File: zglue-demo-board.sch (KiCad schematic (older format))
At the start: 101 parts, among them J10 0473460001, J2 DF13A-2P-1.25H, J3 20021121-00010C4LF, J4 2x20_Header_Female, J5 0473460001, J6 556500488, J7 556500488, J8 WE_686115148922, J9 WE_686115148922, U1 LD1117S33CTR, U2 NTB0104BQ, U3 NTB0104BQ, U4 NTB0104BQ, U5 93LC56CT-IMC, U6 FT4232HQ, Y1 ASFLMB-12.000MHZ-LC-T

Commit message: finished initial component placement, some minor changes in schematics related to footprints
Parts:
- removed C4: C_100n_0402_6V3, antmicro-footprints:0402-cap, symbol antmicroCapacitors0402:C_100n_0402_6V3
- removed C5: C_10u_0603, antmicro-footprints:0603-cap, symbol antmicroCapacitors0603:C_10u_0603
- removed J9: WE_686115148922, antmicro-footprints:WE_686115148922, symbol antmicroFCCConnectors:WE_686115148922
- removed U1: LD1117S33CTR, antmicro-footprints:SOT-223, symbol antmicroPMICVoltageRegulatorsLinear:LD1117S33CTR
- added C4, C5: C_1u_0603, antmicro-footprints:0603-cap, symbol antmicroCapacitors0603:C_1u_0603
- added J9: WE_686115148922_FLIPPED, antmicro-footprints:WE_686115148922_FLIPPED, symbol antmicroFCCConnectors:WE_686115148922_FLIPPED
- added N1: antmicro_logo, antmicro-footprints:antmicro-logo_scaled_20mm, symbol antmicroMechanicalParts:antmicro_logo
- added U1: MCP1700T-3302E_TT, antmicro-footprints:SOT-23-3, symbol antmicroPMICVoltageRegulatorsLinear:MCP1700T-3302E_TT
- FB1, FB2: footprint antmicro-footprints:0603 -> antmicro-footprints:0603-res
- JP1, JP2, JP3: footprint (none) -> Jumper:SolderJumper-3_P1.3mm_Open_Pad1.0x1.5mm
- U5: footprint antmicro-footprints:SOIC-8_W3.9mm -> antmicro-footprints:DFN-8_2x3mm
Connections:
- net labels added: CTRL_RST_FLASH_SOC_CS_3V3
- net labels removed: CTRL_RST, CTRL_RST_3V3
- wire segments 421 -> 418
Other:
- note added: "TODO: check i2c connection\n"
- note added: "Voltage level selection"
- note removed: "TODO: check pin order, check i2c connection\n"
- moved on the sheet: JP1, JP2, JP3, TP5, TP6, TP7

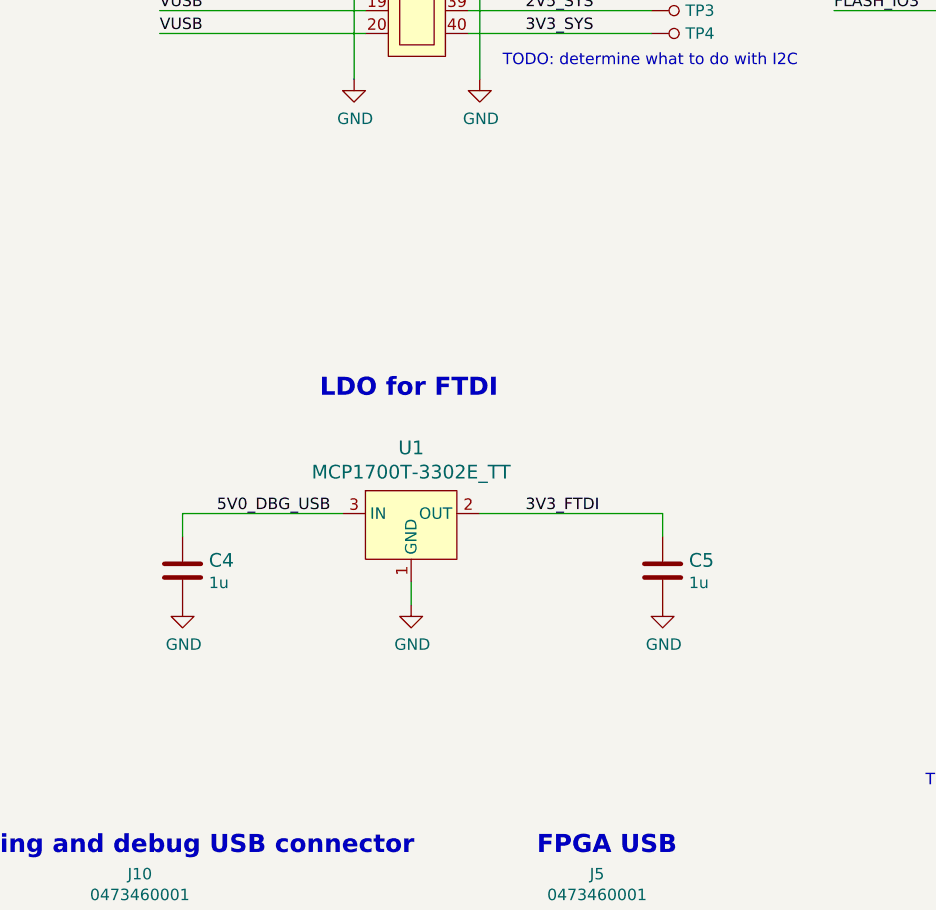
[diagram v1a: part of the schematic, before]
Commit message: added programming header for QSPI flash
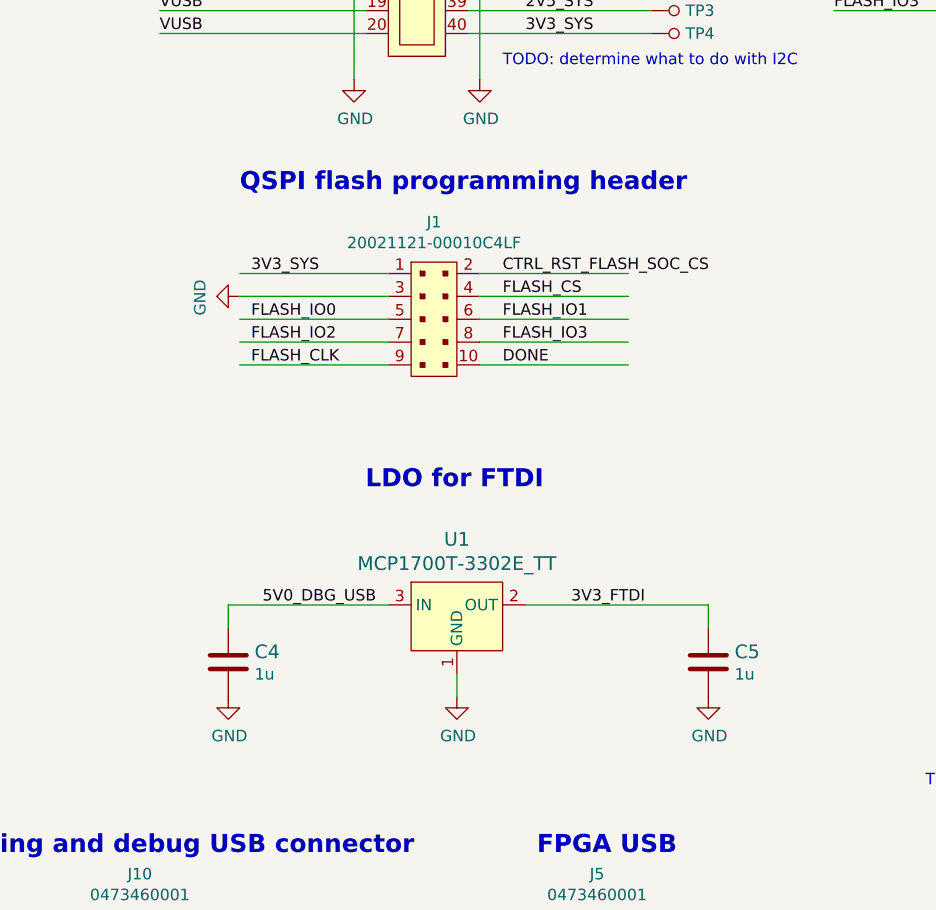
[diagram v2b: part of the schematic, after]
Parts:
- added J1: 20021121-00010C4LF, antmicro-footprints:PinHeader_2x5_P1.27mm, symbol antmicroRectangularConnectorsHeadersMalePins:20021121-00010C4LF
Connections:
- wire segments 418 -> 428
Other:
- note added: "QSPI flash programming header"
- moved on the sheet: C4, C5, U1
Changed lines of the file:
@@
 EESchema Schematic File Version 4
-LIBS:zglue-demo-board-cache
 EELAYER 26 0
 EELAYER END
@@
 L power:GND #PWR07
 U 1 1 5E3C7E24
-P 11400 6000
-F 0 "#PWR07" H 11400 5750 50  0001 C CNN
-F 1 "GND" H 11405 5827 50  0000 C CNN
-F 2 "" H 11400 6000 50  0001 C CNN
-F 3 "" H 11400 6000 50  0001 C CNN
-	1    11400 6000
+P 11600 6400
+F 0 "#PWR07" H 11600 6150 50  0001 C CNN
+F 1 "GND" H 11605 6227 50  0000 C CNN
+F 2 "" H 11600 6400 50  0001 C CNN
+F 3 "" H 11600 6400 50  0001 C CNN
+	1    11600 6400
 	1    0    0    -1
 $EndComp
 Wire Wire Line
-	11400 5900 11400 6000
-Text Label 10550 5600 0    50   ~ 0
+	11600 6300 11600 6400
+Text Label 10750 6000 0    50   ~ 0
 5V0_DBG_USB
-Text Label 11900 5600 0    50   ~ 0
+Text Label 12100 6000 0    50   ~ 0
 3V3_FTDI
-Text Notes 11000 5100 0    79   ~ 16
+Text Notes 11200 5500 0    79   ~ 16
 LDO for FTDI
 $Comp
 L power:GND #PWR06
 U 1 1 5E4D1E3B
-P 10400 6000
-F 0 "#PWR06" H 10400 5750 50  0001 C CNN
-F 1 "GND" H 10405 5827 50  0000 C CNN
-F 2 "" H 10400 6000 50  0001 C CNN
-F 3 "" H 10400 6000 50  0001 C CNN
-	1    10400 6000
+P 10600 6400
+F 0 "#PWR06" H 10600 6150 50  0001 C CNN
+F 1 "GND" H 10605 6227 50  0000 C CNN
+F 2 "" H 10600 6400 50  0001 C CNN
+F 3 "" H 10600 6400 50  0001 C CNN
+	1    10600 6400
 	1    0    0    -1
 $EndComp
@@
 L power:GND #PWR012
 U 1 1 5E4D1F0E
-P 12500 6000
-F 0 "#PWR012" H 12500 5750 50  0001 C CNN
-F 1 "GND" H 12505 5827 50  0000 C CNN
-F 2 "" H 12500 6000 50  0001 C CNN
-F 3 "" H 12500 6000 50  0001 C CNN
-	1    12500 6000
+P 12700 6400
+F 0 "#PWR012" H 12700 6150 50  0001 C CNN
+F 1 "GND" H 12705 6227 50  0000 C CNN
+F 2 "" H 12700 6400 50  0001 C CNN
+F 3 "" H 12700 6400 50  0001 C CNN
+	1    12700 6400
 	1    0    0    -1
 $EndComp
 Wire Wire Line
-	10400 5600 11100 5600
+	10600 6000 11300 6000
 $Comp
 L antmicroDiodesRectifiersSingle:MBR0540T1G D1
@@
 L antmicroPMICVoltageRegulatorsLinear:MCP1700T-3302E_TT U1
 U 1 1 5DD3D3B5
-P 11400 5600
-F 0 "U1" H 11400 5887 60  0000 C CNN
-F 1 "MCP1700T-3302E_TT" H 11400 5781 60  0000 C CNN
-F 2 "antmicro-footprints:SOT-23-3" H 11600 5800 60  0001 L CNN
-F 3 "http://www.microchip.com/mymicrochip/filehandler.aspx?ddocname=en011779" H 11600 5900 60  0001 L CNN
-F 4 "MCP1700T-3302E/TT" H 11600 6100 60  0001 L CNN "MPN"
-F 5 "Microchip Technology" H 11600 6700 60  0001 L CNN "Manufacturer"
-	1    11400 5600
+P 11600 6000
+F 0 "U1" H 11600 6287 60  0000 C CNN
+F 1 "MCP1700T-3302E_TT" H 11600 6181 60  0000 C CNN
+F 2 "antmicro-footprints:SOT-23-3" H 11800 6200 60  0001 L CNN
+F 3 "http://www.microchip.com/mymicrochip/filehandler.aspx?ddocname=en011779" H 11800 6300 60  0001 L CNN
+F 4 "MCP1700T-3302E/TT" H 11800 6500 60  0001 L CNN "MPN"
+F 5 "Microchip Technology" H 11800 7100 60  0001 L CNN "Manufacturer"
+	1    11600 6000
 	1    0    0    -1
 $EndComp
 Wire Wire Line
-	11700 5600 12500 5600
+	11900 6000 12700 6000
 $Comp
 L antmicroCapacitors0603:C_1u_0603 C4
 U 1 1 5DD84060
-P 10400 5850
-F 0 "C4" H 10515 5895 60  0000 L CNN
-F 1 "C_1u_0603" H 10400 5700 60  0001 C CNN
-F 2 "antmicro-footprints:0603-cap" H 10600 6050 60  0001 L CNN
-F 3 "" H 10400 5850 50  0001 C CNN
-F 4 "WALSIN" H 10600 6250 60  0001 L CNN "Manufacturer"
-F 5 "0603X105K160CT" H 10600 6150 60  0001 L CNN "MPN"
-F 6 "1u" H 10515 5797 50  0000 L CNN "Val"
-	1    10400 5850
+P 10600 6250
+F 0 "C4" H 10715 6295 60  0000 L CNN
+F 1 "C_1u_0603" H 10600 6100 60  0001 C CNN
+F 2 "antmicro-footprints:0603-cap" H 10800 6450 60  0001 L CNN
+F 3 "" H 10600 6250 50  0001 C CNN
+F 4 "WALSIN" H 10800 6650 60  0001 L CNN "Manufacturer"
+F 5 "0603X105K160CT" H 10800 6550 60  0001 L CNN "MPN"
+F 6 "1u" H 10715 6197 50  0000 L CNN "Val"
+	1    10600 6250
 	1    0    0    -1
 $EndComp
 Wire Wire Line
-	10400 5600 10400 5700
+	10600 6000 10600 6100
 Wire Wire Line
-	12500 5600 12500 5700
+	12700 6000 12700 6100
 $Comp
 L antmicroCapacitors0603:C_1u_0603 C5
 U 1 1 5DDC8C57
-P 12500 5850
-F 0 "C5" H 12615 5895 60  0000 L CNN
-F 1 "C_1u_0603" H 12500 5700 60  0001 C CNN
-F 2 "antmicro-footprints:0603-cap" H 12700 6050 60  0001 L CNN
-F 3 "" H 12500 5850 50  0001 C CNN
-F 4 "WALSIN" H 12700 6250 60  0001 L CNN "Manufacturer"
-F 5 "0603X105K160CT" H 12700 6150 60  0001 L CNN "MPN"
-F 6 "1u" H 12615 5797 50  0000 L CNN "Val"
-	1    12500 5850
+P 12700 6250
+F 0 "C5" H 12815 6295 60  0000 L CNN
+F 1 "C_1u_0603" H 12700 6100 60  0001 C CNN
+F 2 "antmicro-footprints:0603-cap" H 12900 6450 60  0001 L CNN
+F 3 "" H 12700 6250 50  0001 C CNN
+F 4 "WALSIN" H 12900 6650 60  0001 L CNN "Manufacturer"
+F 5 "0603X105K160CT" H 12900 6550 60  0001 L CNN "MPN"
+F 6 "1u" H 12815 6197 50  0000 L CNN "Val"
+	1    12700 6250
 	1    0    0    -1
 $EndComp
@@
 	1    0    0    -1
 $EndComp
+$Comp
+L antmicroRectangularConnectorsHeadersMalePins:20021121-00010C4LF J1
+U 1 1 5DB8DE82
+P 11500 4750
+F 0 "J1" H 11500 5175 50  0000 C CNN
+F 1 "20021121-00010C4LF" H 11500 5084 50  0000 C CNN
+F 2 "antmicro-footprints:PinHeader_2x5_P1.27mm" H 11700 4950 60  0001 L CNN
+F 3 "https://cdn.amphenol-icc.com/media/wysiwyg/files/drawing/20021121.pdf" H 11700 5050 60  0001 L CNN
+F 4 "20021121-00010C4LF" H 11700 5250 60  0001 L CNN "MPN"
+F 5 "Amphenol ICC (FCI)" H 11700 5850 60  0001 L CNN "Manufacturer"
+	1    11500 4750
+	1    0    0    -1
+$EndComp
+Wire Wire Line
+	11300 4550 10650 4550
+Wire Wire Line
+	11300 4650 10650 4650
+Wire Wire Line
+	11300 4750 10650 4750
+Wire Wire Line
+	11300 4850 10650 4850
+Wire Wire Line
+	11300 4950 10650 4950
+Wire Wire Line
+	12350 4550 11700 4550
+Wire Wire Line
+	12350 4650 11700 4650
+Wire Wire Line
+	12350 4750 11700 4750
+Wire Wire Line
+	12350 4850 11700 4850
+Wire Wire Line
+	12350 4950 11700 4950
+Text Label 10700 4750 0    50   ~ 0
+FLASH_IO0
+Text Label 11800 4750 0    50   ~ 0
+FLASH_IO1
+Text Label 10700 4850 0    50   ~ 0
+FLASH_IO2
+Text Label 11800 4850 0    50   ~ 0
+FLASH_IO3
+Text Label 11800 4550 0    50   ~ 0
+CTRL_RST_FLASH_SOC_CS
+Text Label 11800 4650 0    50   ~ 0
+FLASH_CS
+Text Label 10700 4950 0    50   ~ 0
+FLASH_CLK
+Text Label 11800 4950 0    50   ~ 0
+DONE
+Text Label 10700 4550 0    50   ~ 0
+3V3_SYS
+$Comp
+L power:GND #PWR?
+U 1 1 5DF0D91A
+P 10650 4650
+F 0 "#PWR?" H 10650 4400 50  0001 C CNN
+F 1 "GND" H 10655 4477 50  0000 C CNN
+F 2 "" H 10650 4650 50  0001 C CNN
+F 3 "" H 10650 4650 50  0001 C CNN
+	1    10650 4650
+	0    1    1    0
+$EndComp
+Text Notes 10650 4200 0    79   ~ 16
+QSPI flash programming header
 $EndSCHEMATC

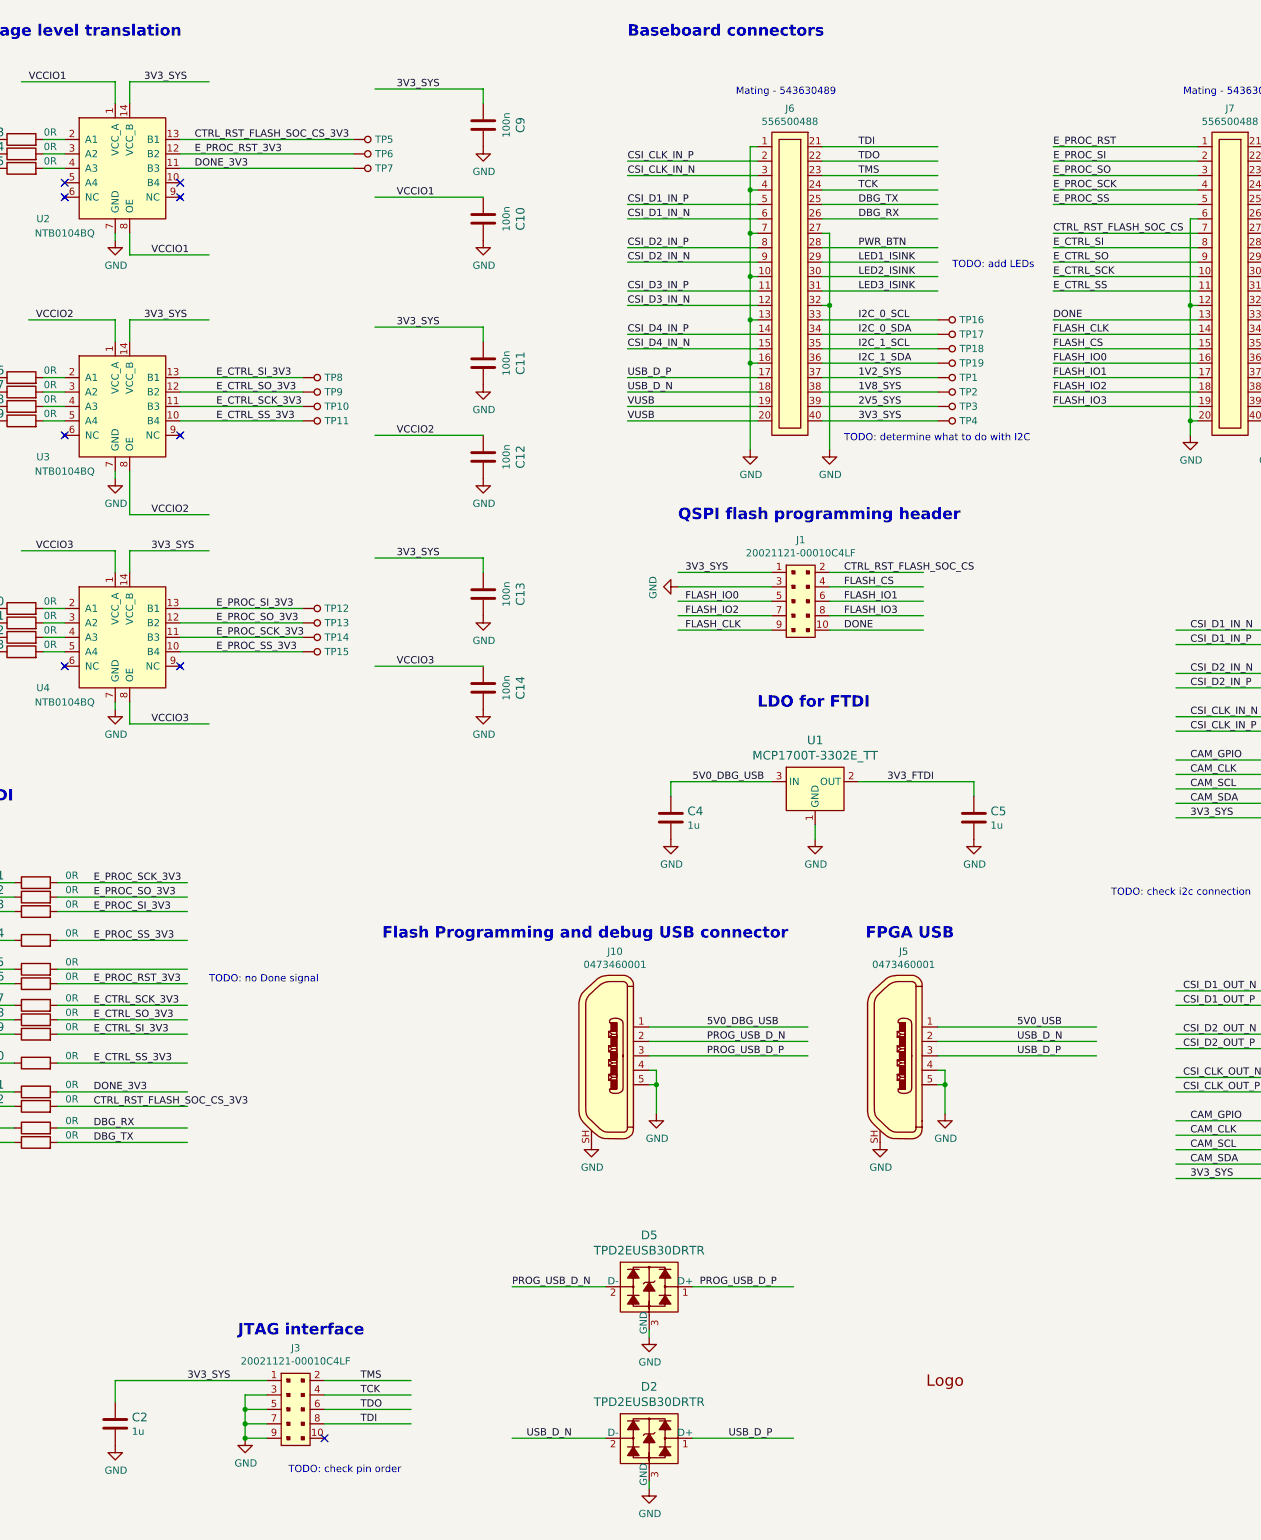
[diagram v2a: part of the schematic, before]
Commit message: added LEDs and power button
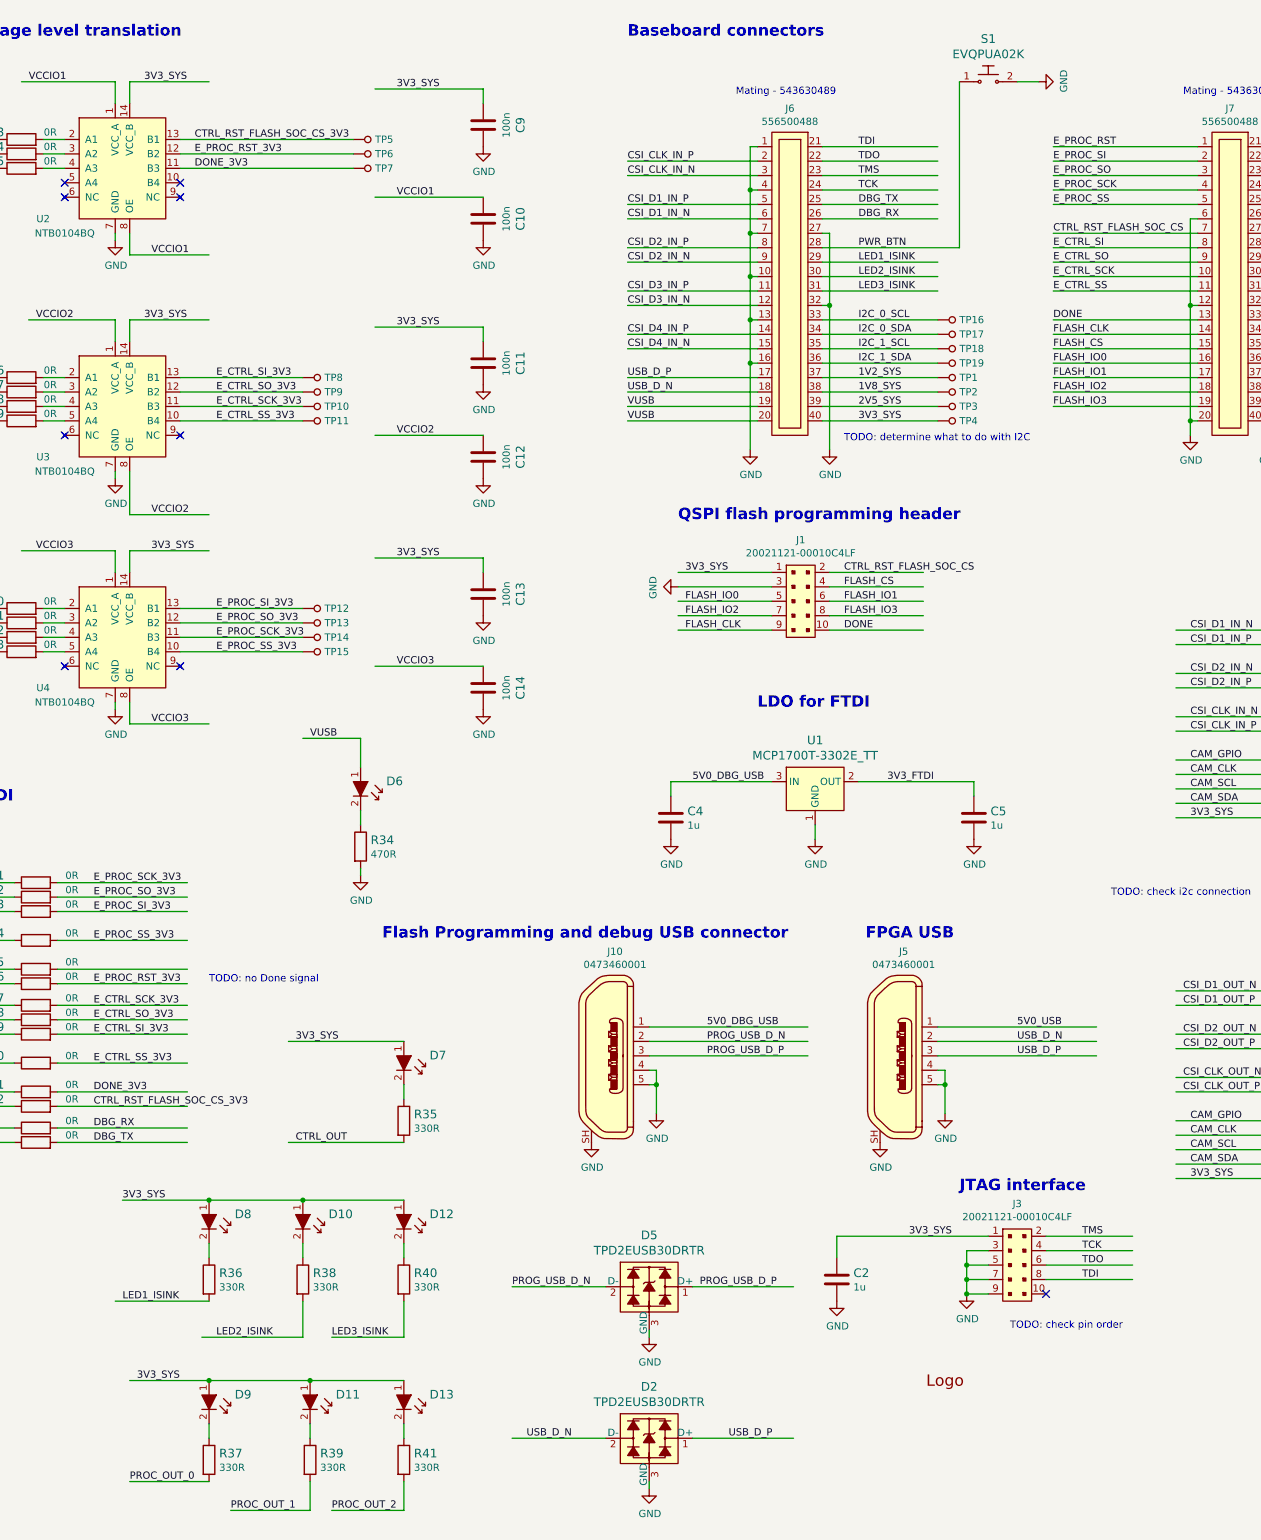
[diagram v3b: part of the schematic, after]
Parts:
- added D10, D11, D12, D13, D6, D7, D8, D9: LG_L29K-G2J1-24-Z, antmicro-footprints:LED_0603, symbol antmicroLEDIndicationDiscrete:LG_L29K-G2J1-24-Z
- added R34: R_470R_0402, antmicro-footprints:0402-res, symbol antmicroResistors0402:R_470R_0402
- added R35, R36, R37, R38, R39, R40, R41: R_330R_0402, antmicro-footprints:0402-res, symbol antmicroResistors0402:R_330R_0402
- added S1: EVQPUA02K, antmicro-footprints:Panasonic_EVQPUJ_EVQPUA, symbol antmicroTactileSwitches:EVQPUA02K
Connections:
- wire segments 428 -> 459
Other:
- note removed: "TODO: add LEDs\n"
- moved on the sheet: C2, J3

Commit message: Added connections for I2C and UART
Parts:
- added R42, R43, R44, R45, R46, R47, R48, R49, R50, R51, R52, R53, R54, R55, R56, R57: R_0R_0402, antmicro-footprints:0402-res, symbol antmicroResistors0402:R_0R_0402
- added TP20, TP21, TP22, TP23: TP_SMD1MM, antmicro-footprints:Testpoint_smd_1mm, symbol antmicroTestPoints:TP_SMD1MM
- added U7, U8: NTB0104BQ, antmicro-footprints:QDHVQFN14, symbol antmicroLogicTranslatorsLevelShifters:NTB0104BQ
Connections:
- net labels added: CAM_CLK_IN, CAM_CLK_OUT, CAM_GPIO_IN, CAM_GPIO_OUT, CAM_SCL_IN, CAM_SCL_OUT, CAM_SDA_IN, CAM_SDA_OUT, DBG_RX_3V3, DBG_TX_3V3, I2C_0_SCL_3V3, I2C_0_SDA_3V3, I2C_1_SCL_3V3, I2C_1_SDA_3V3, RPI_SCL, RPI_SDA
- net labels removed: CAM_CLK, CAM_GPIO, CAM_SCL, CAM_SDA
- wire segments 459 -> 516
- no-connect marks 27 -> 59
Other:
- note removed: "TODO: check i2c connection\n"
- moved on the sheet: C2, C3, C4, C5, D10, D11, D12, D13, D2, D5, D6, D8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
